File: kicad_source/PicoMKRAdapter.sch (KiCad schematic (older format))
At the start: 3 parts, among them CN1 RASPBERRYPI_PICO, CN2 ARDUINO_MKR, CN3 CONN_01X04

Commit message: added layout
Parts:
- added L1, L2: Label, labels:generationmake_logo, symbol devices:Label
- CN2: footprint MODULE_compute:ARDUINO_MKR -> MODULE_compute:ARDUINO_MKR_BASEBOARD
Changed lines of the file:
@@
 F 0 "CN2" H 6050 2847 60  0000 C CNN
 F 1 "ARDUINO_MKR" H 6050 2741 60  0000 C CNN
-F 2 "MODULE_compute:ARDUINO_MKR" H 5950 2600 60  0001 C CNN
+F 2 "MODULE_compute:ARDUINO_MKR_BASEBOARD" H 5950 2600 60  0001 C CNN
 F 3 "" H 6050 1650 60  0000 C CNN
 	1    6050 1950
@@
 $EndComp
 $Comp
-L power-supply:GND #PWR?
+L power-supply:GND #PWR01
 U 1 1 600DC642
 P 4500 5300
-F 0 "#PWR?" H 4500 5050 50  0001 C CNN
+F 0 "#PWR01" H 4500 5050 50  0001 C CNN
 F 1 "GND" H 4500 5150 50  0000 C CNN
 F 2 "" H 4500 5300 50  0000 C CNN
@@
 $EndComp
 $Comp
-L power-supply:GND #PWR?
+L power-supply:GND #PWR02
 U 1 1 600DCEAA
 P 7800 5300
-F 0 "#PWR?" H 7800 5050 50  0001 C CNN
+F 0 "#PWR02" H 7800 5050 50  0001 C CNN
 F 1 "GND" H 7800 5150 50  0000 C CNN
 F 2 "" H 7800 5300 50  0000 C CNN
@@
 	8450 3300 7700 3300
 $Comp
-L power-supply:+3.3V #PWR?
+L power-supply:+3.3V #PWR03
 U 1 1 600E8877
 P 7900 3200
-F 0 "#PWR?" H 7900 3050 50  0001 C CNN
+F 0 "#PWR03" H 7900 3050 50  0001 C CNN
 F 1 "+3.3V" H 7900 3340 50  0000 C CNN
 F 2 "" H 7900 3200 50  0000 C CNN
@@
 Text Label 7900 4600 0    60   ~ 0
 A6
+$Comp
+L devices:Label L2
+U 1 1 600D2B37
+P 750 7600
+F 0 "L2" H 978 7706 60  0000 L CNN
+F 1 "Label" H 978 7600 60  0000 L CNN
+F 2 "labels:generationmake_logo" H 978 7494 60  0000 L CNN
+F 3 "" H 750 7600 60  0000 C CNN
+	1    750  7600
+	1    0    0    -1
+$EndComp
+$Comp
+L devices:Label L1
+U 1 1 600D30AE
+P 750 7250
+F 0 "L1" H 978 7356 60  0000 L CNN
+F 1 "Label" H 978 7250 60  0000 L CNN
+F 2 "labels:generationmake_logo" H 978 7144 60  0000 L CNN
+F 3 "" H 750 7250 60  0000 C CNN
+	1    750  7250
+	1    0    0    -1
+$EndComp
 $EndSCHEMATC

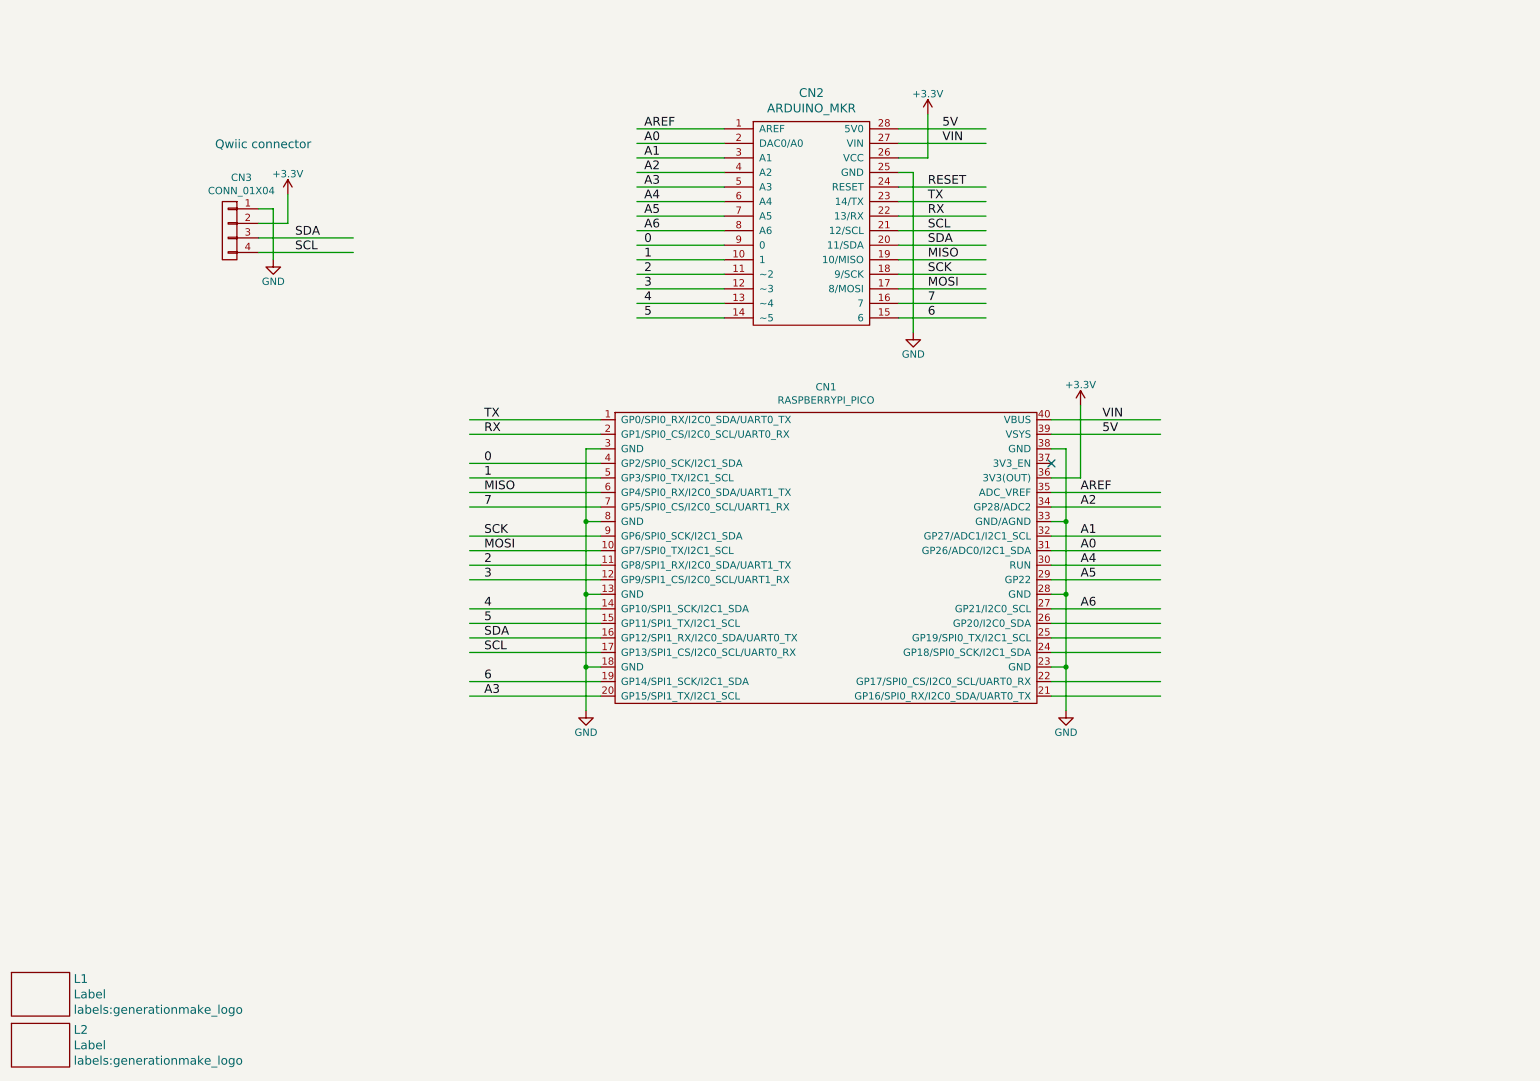
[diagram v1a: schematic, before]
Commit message: updated layout and schematic, added i2c and serial connectors
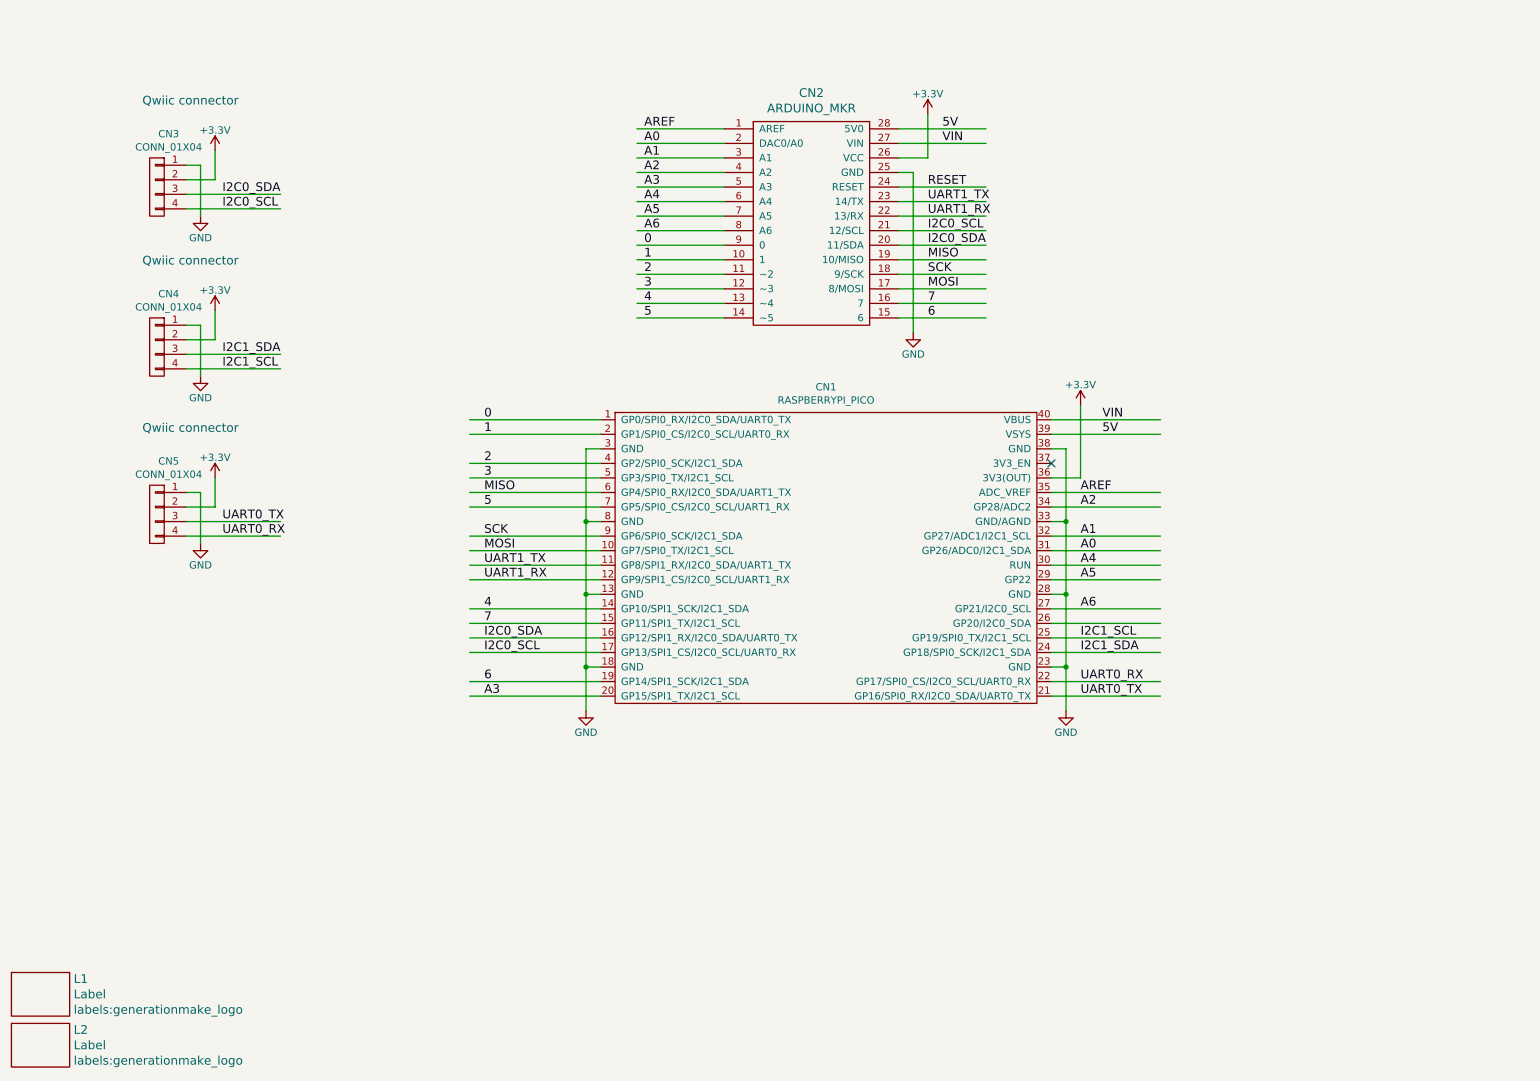
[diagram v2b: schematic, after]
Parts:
- added CN4, CN5: CONN_01X04, connectors_JST_SH:Connectors_JST_SM04B-SRSS-TB, symbol mechanical-connectors:CONN_01X04
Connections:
- net labels added: I2C0_SCL, I2C0_SDA, I2C1_SCL, I2C1_SDA, UART0_RX, UART0_TX, UART1_RX, UART1_TX
- net labels removed: RX, SCL, SDA, TX
- wire segments 84 -> 96
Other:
- moved on the sheet: CN3
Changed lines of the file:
@@
 Sheet 1 1
 Title "PicoMKRAdapter"
-Date "2021-01-24"
+Date "2021-01-25"
 Rev "0.1"
 Comp "generationmake"
@@
 L mechanical-connectors:CONN_01X04 CN3
 U 1 1 5CB452DC
-P 2050 2000
-F 0 "CN3" H 1969 2365 50  0000 C CNN
-F 1 "CONN_01X04" H 1969 2274 50  0000 C CNN
-F 2 "connectors_JST_SH:Connectors_JST_SM04B-SRSS-TB" H 1969 2273 50  0001 C CNN
-F 3 "" H 2050 2000 50  0000 C CNN
-	1    2050 2000
+P 1550 1700
+F 0 "CN3" H 1469 2065 50  0000 C CNN
+F 1 "CONN_01X04" H 1469 1974 50  0000 C CNN
+F 2 "connectors_JST_SH:Connectors_JST_SM04B-SRSS-TB" H 1469 1973 50  0001 C CNN
+F 3 "" H 1550 1700 50  0000 C CNN
+	1    1550 1700
 	-1   0    0    -1
 $EndComp
@@
 L power-supply:GND #PWR0101
 U 1 1 5CB46465
-P 2350 2200
-F 0 "#PWR0101" H 2350 1950 50  0001 C CNN
-F 1 "GND" H 2350 2050 50  0000 C CNN
-F 2 "" H 2350 2200 50  0000 C CNN
-F 3 "" H 2350 2200 50  0000 C CNN
-	1    2350 2200
+P 1850 1900
+F 0 "#PWR0101" H 1850 1650 50  0001 C CNN
+F 1 "GND" H 1850 1750 50  0000 C CNN
+F 2 "" H 1850 1900 50  0000 C CNN
+F 3 "" H 1850 1900 50  0000 C CNN
+	1    1850 1900
 	1    0    0    -1
 $EndComp
@@
 L power-supply:+3.3V #PWR0102
 U 1 1 5CB4647E
-P 2450 1750
-F 0 "#PWR0102" H 2450 1600 50  0001 C CNN
-F 1 "+3.3V" H 2450 1890 50  0000 C CNN
-F 2 "" H 2450 1750 50  0000 C CNN
-F 3 "" H 2450 1750 50  0000 C CNN
-	1    2450 1750
-	1    0    0    -1
-$EndComp
-Wire Wire Line
-	2900 2050 2250 2050
-Wire Wire Line
-	2900 2150 2250 2150
-Wire Wire Line
-	2450 1950 2450 1750
-Wire Wire Line
-	2250 1950 2450 1950
-Wire Wire Line
-	2250 1850 2350 1850
-Wire Wire Line
-	2350 1850 2350 2200
-Text Label 2500 2050 0    60   ~ 0
-SDA
-Text Label 2500 2150 0    60   ~ 0
-SCL
-Text Notes 1950 1450 0    60   ~ 0
+P 1950 1450
+F 0 "#PWR0102" H 1950 1300 50  0001 C CNN
+F 1 "+3.3V" H 1950 1590 50  0000 C CNN
+F 2 "" H 1950 1450 50  0000 C CNN
+F 3 "" H 1950 1450 50  0000 C CNN
+	1    1950 1450
+	1    0    0    -1
+$EndComp
+Wire Wire Line
+	2400 1750 1750 1750
+Wire Wire Line
+	2400 1850 1750 1850
+Wire Wire Line
+	1950 1650 1950 1450
+Wire Wire Line
+	1750 1650 1950 1650
+Wire Wire Line
+	1750 1550 1850 1550
+Wire Wire Line
+	1850 1550 1850 1900
+Text Label 2000 1750 0    60   ~ 0
+I2C0_SDA
+Text Label 2000 1850 0    60   ~ 0
+I2C0_SCL
+Text Notes 1450 1150 0    60   ~ 0
 Qwiic connector
 $Comp
@@
 RESET
 Text Label 6850 1800 0    60   ~ 0
-TX
+UART1_TX
 Text Label 6850 1900 0    60   ~ 0
-RX
-Text Label 6850 2000 0    60   ~ 0
-SCL
-Text Label 6850 2100 0    60   ~ 0
-SDA
+UART1_RX
 Wire Wire Line
 	7250 2200 6650 2200
@@
 Text Label 3800 4200 0    60   ~ 0
 MOSI
-Text Label 3800 3300 0    60   ~ 0
-TX
-Text Label 3800 3400 0    60   ~ 0
-RX
-Text Label 3800 4900 0    60   ~ 0
-SCL
-Text Label 3800 4800 0    60   ~ 0
-SDA
+Text Label 7900 5200 0    60   ~ 0
+UART0_TX
+Text Label 7900 5100 0    60   ~ 0
+UART0_RX
 Text Label 7900 3800 0    60   ~ 0
 AREF
@@
 Wire Wire Line
 	8450 4400 7700 4400
-Text Label 3800 3900 0    60   ~ 0
+Text Label 3800 4700 0    60   ~ 0
 7
+Text Label 3800 3300 0    60   ~ 0
+0
+Text Label 3800 3400 0    60   ~ 0
+1
 Text Label 3800 3600 0    60   ~ 0
-0
+2
 Text Label 3800 3700 0    60   ~ 0
-1
-Text Label 3800 4300 0    60   ~ 0
-2
-Text Label 3800 4400 0    60   ~ 0
 3
 Text Label 3800 4600 0    60   ~ 0
 4
-Text Label 3800 4700 0    60   ~ 0
+Text Label 3800 3900 0    60   ~ 0
 5
 Text Label 3800 5100 0    60   ~ 0
@@
 	1    0    0    -1
 $EndComp
+Text Label 6850 2100 0    60   ~ 0
+I2C0_SDA
+Text Label 6850 2000 0    60   ~ 0
+I2C0_SCL
+Text Label 3800 4800 0    60   ~ 0
+I2C0_SDA
+Text Label 3800 4900 0    60   ~ 0
+I2C0_SCL
+Text Label 7900 4800 0    60   ~ 0
+I2C1_SCL
+Text Label 7900 4900 0    60   ~ 0
+I2C1_SDA
+Text Label 3800 4400 0    60   ~ 0
+UART1_RX
+Text Label 3800 4300 0    60   ~ 0
+UART1_TX
+$Comp
+L mechanical-connectors:CONN_01X04 CN4
+U 1 1 600F6423
+P 1550 2800
+F 0 "CN4" H 1469 3165 50  0000 C CNN
+F 1 "CONN_01X04" H 1469 3074 50  0000 C CNN
+F 2 "connectors_JST_SH:Connectors_JST_SM04B-SRSS-TB" H 1469 3073 50  0001 C CNN
+F 3 "" H 1550 2800 50  0000 C CNN
+	1    1550 2800
+	-1   0    0    -1
+$EndComp
+$Comp
+L power-supply:GND #PWR04
+U 1 1 600F653B
+P 1850 3000
+F 0 "#PWR04" H 1850 2750 50  0001 C CNN
+F 1 "GND" H 1850 2850 50  0000 C CNN
+F 2 "" H 1850 3000 50  0000 C CNN
+F 3 "" H 1850 3000 50  0000 C CNN
+	1    1850 3000
+	1    0    0    -1
+$EndComp
+$Comp
+L power-supply:+3.3V #PWR06
+U 1 1 600F6545
+P 1950 2550
+F 0 "#PWR06" H 1950 2400 50  0001 C CNN
+F 1 "+3.3V" H 1950 2690 50  0000 C CNN
+F 2 "" H 1950 2550 50  0000 C CNN
+F 3 "" H 1950 2550 50  0000 C CNN
+	1    1950 2550
+	1    0    0    -1
+$EndComp
+Wire Wire Line
+	2400 2850 1750 2850
+Wire Wire Line
+	2400 2950 1750 2950
+Wire Wire Line
+	1950 2750 1950 2550
+Wire Wire Line
+	1750 2750 1950 2750
+Wire Wire Line
+	1750 2650 1850 2650
+Wire Wire Line
+	1850 2650 1850 3000
+Text Label 2000 2850 0    60   ~ 0
+I2C1_SDA
+Text Label 2000 2950 0    60   ~ 0
+I2C1_SCL
+Text Notes 1450 2250 0    60   ~ 0
+Qwiic connector
+$Comp
+L mechanical-connectors:CONN_01X04 CN5
+U 1 1 600FDD13
+P 1550 3950
+F 0 "CN5" H 1469 4315 50  0000 C CNN
+F 1 "CONN_01X04" H 1469 4224 50  0000 C CNN
+F 2 "connectors_JST_SH:Connectors_JST_SM04B-SRSS-TB" H 1469 4223 50  0001 C CNN
+F 3 "" H 1550 3950 50  0000 C CNN
+	1    1550 3950
+	-1   0    0    -1
+$EndComp
+$Comp
+L power-supply:GND #PWR05
+U 1 1 600FDE75
+P 1850 4150
+F 0 "#PWR05" H 1850 3900 50  0001 C CNN
+F 1 "GND" H 1850 4000 50  0000 C CNN
+F 2 "" H 1850 4150 50  0000 C CNN
+F 3 "" H 1850 4150 50  0000 C CNN
+	1    1850 4150
+	1    0    0    -1
+$EndComp
+$Comp
+L power-supply:+3.3V #PWR07
+U 1 1 600FDE7F
+P 1950 3700
+F 0 "#PWR07" H 1950 3550 50  0001 C CNN
+F 1 "+3.3V" H 1950 3840 50  0000 C CNN
+F 2 "" H 1950 3700 50  0000 C CNN
+F 3 "" H 1950 3700 50  0000 C CNN
+	1    1950 3700
+	1    0    0    -1
+$EndComp
+Wire Wire Line
+	2400 4000 1750 4000
+Wire Wire Line
+	2400 4100 1750 4100
+Wire Wire Line
+	1950 3900 1950 3700
+Wire Wire Line
+	1750 3900 1950 3900
+Wire Wire Line
+	1750 3800 1850 3800
+Wire Wire Line
+	1850 3800 1850 4150
+Text Notes 1450 3400 0    60   ~ 0
+Qwiic connector
+Text Label 2000 4100 0    60   ~ 0
+UART0_RX
+Text Label 2000 4000 0    60   ~ 0
+UART0_TX
 $EndSCHEMATC

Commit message: connected RUN to RESET, added some labels
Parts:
- added L3: Label, Symbol:OSHW-Symbol_6.7x6mm_SilkScreen, symbol devices:Label
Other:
- note added: "3V3_EN needs no connection \nbecause it is pulled up on the Raspberry Pi Pico"
- note added: "find full project documentation at https://github.com/generationmake/PicoMKRAdapter"
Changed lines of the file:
@@
 Sheet 1 1
 Title "PicoMKRAdapter"
-Date "2021-01-25"
+Date "2021-01-27"
 Rev "0.1"
 Comp "generationmake"
@@
 Text Label 3800 5200 0    60   ~ 0
 A3
-Text Label 7900 4300 0    60   ~ 0
+Text Label 7900 4400 0    60   ~ 0
 A4
-Text Label 7900 4400 0    60   ~ 0
+Text Label 7900 4600 0    60   ~ 0
 A5
-Text Label 7900 4600 0    60   ~ 0
+Text Label 7900 4700 0    60   ~ 0
 A6
 $Comp
@@
 Text Label 2000 4000 0    60   ~ 0
 UART0_TX
+Text Label 7900 4300 0    60   ~ 0
+RESET
+Text Notes 8250 3700 0    60   ~ 0
+3V3_EN needs no connection \nbecause it is pulled up on the Raspberry Pi Pico
+Text Notes 550  600  0    60   ~ 0
+find full project documentation at https://github.com/generationmake/PicoMKRAdapter
+$Comp
+L devices:Label L3
+U 1 1 60120086
+P 750 6900
+F 0 "L3" H 978 7006 60  0000 L CNN
+F 1 "Label" H 978 6900 60  0000 L CNN
+F 2 "Symbol:OSHW-Symbol_6.7x6mm_SilkScreen" H 978 6794 60  0000 L CNN
+F 3 "" H 750 6900 60  0000 C CNN
+	1    750  6900
+	1    0    0    -1
+$EndComp
 $EndSCHEMATC

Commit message: updated pdfs and images
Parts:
- CN3, CN4, CN5: value CONN_01X04 -> SM04B-SRSS-TB
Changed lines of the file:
@@
 P 1550 1700
 F 0 "CN3" H 1469 2065 50  0000 C CNN
-F 1 "CONN_01X04" H 1469 1974 50  0000 C CNN
+F 1 "SM04B-SRSS-TB" H 1469 1974 50  0000 C CNN
 F 2 "connectors_JST_SH:Connectors_JST_SM04B-SRSS-TB" H 1469 1973 50  0001 C CNN
 F 3 "" H 1550 1700 50  0000 C CNN
@@
 P 1550 2800
 F 0 "CN4" H 1469 3165 50  0000 C CNN
-F 1 "CONN_01X04" H 1469 3074 50  0000 C CNN
+F 1 "SM04B-SRSS-TB" H 1469 3074 50  0000 C CNN
 F 2 "connectors_JST_SH:Connectors_JST_SM04B-SRSS-TB" H 1469 3073 50  0001 C CNN
 F 3 "" H 1550 2800 50  0000 C CNN
@@
 P 1550 3950
 F 0 "CN5" H 1469 4315 50  0000 C CNN
-F 1 "CONN_01X04" H 1469 4224 50  0000 C CNN
+F 1 "SM04B-SRSS-TB" H 1469 4224 50  0000 C CNN
 F 2 "connectors_JST_SH:Connectors_JST_SM04B-SRSS-TB" H 1469 4223 50  0001 C CNN
 F 3 "" H 1550 3950 50  0000 C CNN
